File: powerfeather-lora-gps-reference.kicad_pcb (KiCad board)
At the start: 2 copper layers, 23.1 x 58.1 mm, 19 parts, among them J1 Conn_01x05, J10 Conn_01x01, J11 Conn_01x04, J2 Conn_01x02, J3 Conn_01x04, J4 Conn_01x02, J5 Conn_01x02, J6 Conn_01x04, J7 Conn_01x04, J8 Conn_01x03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

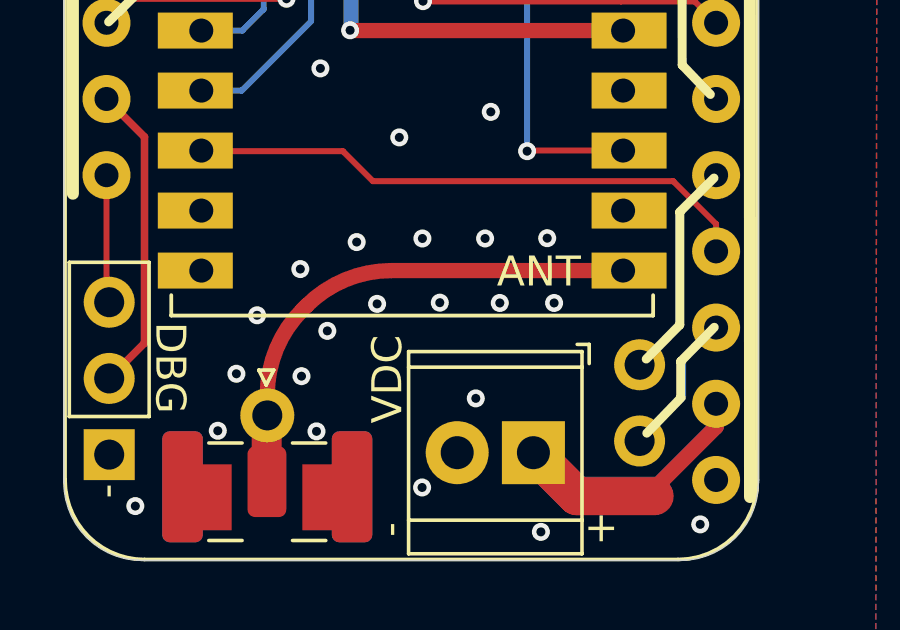
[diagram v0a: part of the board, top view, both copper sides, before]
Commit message: Change antenna trace width according to calc
- 4.5 dielectric constant
- H=1.6
- 865/920 Mhz
- S=0.5
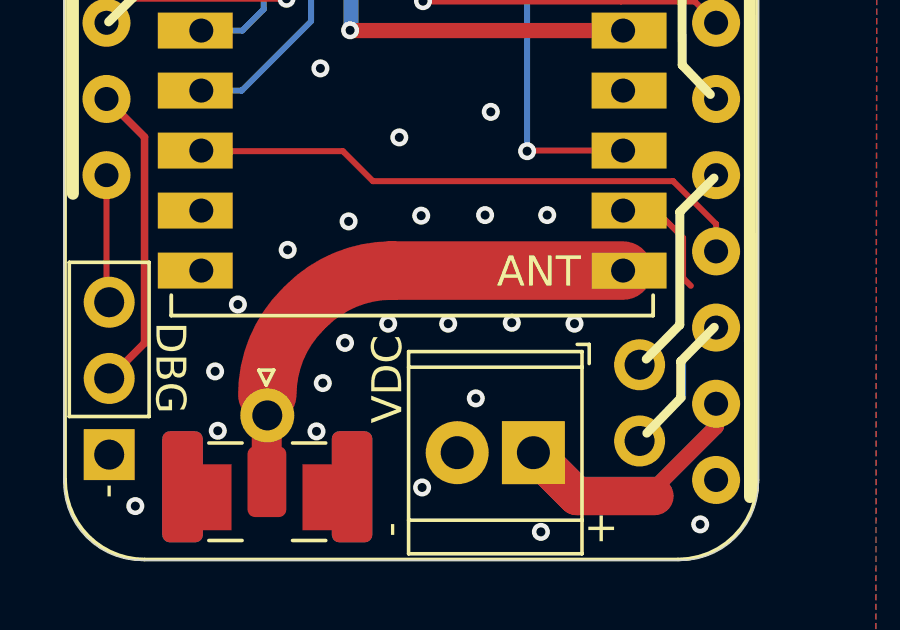
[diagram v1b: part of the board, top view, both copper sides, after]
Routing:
- net GND: track 2.11 -> 6.20 mm
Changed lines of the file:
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@@
+	)
+	(segment
+		(start 140.19 116.834365)
+		(end 140.19 118.18)
+		(width 0.2)
+		(layer "F.Cu")
+		(net 1)
+	)
+	(segment
+		(start 139.285635 115.93)
+		(end 140.19 116.834365)
+		(width 0.2)
+		(layer "F.Cu")
+		(net 1)
 	)
 	(segment
@@
 		(net 1)
 	)
-	(via
-		(at 129.99 119.04)
+	(segment
+		(start 138.19 115.93)
+		(end 139.285635 115.93)
+		(width 0.2)
+		(layer "F.Cu")
+		(net 1)
+	)
+	(segment
+		(start 140.19 118.18)
+		(end 140.45 118.44)
+		(width 0.2)
+		(layer "F.Cu")
+		(net 1)
+	)
+	(via
+		(at 130.36 119.7)
 		(size 0.6)
 		(drill 0.3)
@@
 	)
 	(via
-		(at 134.08 119.01)
+		(at 134.48 119.67)
 		(size 0.6)
 		(drill 0.3)
@@
 	)
 	(via
-		(at 129.31 116.98)
-		(size 0.6)
-		(drill 0.3)
-		(layers "F.Cu" "B.Cu")
-		(free yes)
-		(net 1)
-	)
-	(via
-		(at 128.33 119.94)
+		(at 129.04 116.29)
+		(size 0.6)
+		(drill 0.3)
+		(layers "F.Cu" "B.Cu")
+		(free yes)
+		(net 1)
+	)
+	(via
+		(at 128.92 120.34)
 		(size 0.6)
 		(drill 0.3)
@@
 	)
 	(via
-		(at 131.5 116.86)
+		(at 131.46 116.1)
 		(size 0.6)
 		(drill 0.3)
@@
 	)
 	(via
-		(at 135.89 119.01)
-		(size 0.6)
-		(drill 0.3)
-		(layers "F.Cu" "B.Cu")
-		(free yes)
-		(net 1)
-	)
-	(via
-		(at 133.59 116.86)
-		(size 0.6)
-		(drill 0.3)
-		(layers "F.Cu" "B.Cu")
-		(free yes)
-		(net 1)
-	)
-	(via
-		(at 127.43 117.88)
-		(size 0.6)
-		(drill 0.3)
-		(layers "F.Cu" "B.Cu")
-		(free yes)
-		(net 1)
-	)
-	(via
-		(at 135.66 116.85)
+		(at 136.57 119.7)
+		(size 0.6)
+		(drill 0.3)
+		(layers "F.Cu" "B.Cu")
+		(free yes)
+		(net 1)
+	)
+	(via
+		(at 133.59 116.08)
+		(size 0.6)
+		(drill 0.3)
+		(layers "F.Cu" "B.Cu")
+		(free yes)
+		(net 1)
+	)
+	(via
+		(at 127.01 117.24)
+		(size 0.6)
+		(drill 0.3)
+		(layers "F.Cu" "B.Cu")
+		(free yes)
+		(net 1)
+	)
+	(via
+		(at 135.66 116.08)
 		(size 0.6)
 		(drill 0.3)
@@
 	)
 	(via
-		(at 125.99 119.42)
+		(at 125.35 119.06)
 		(size 0.6)
 		(drill 0.3)
@@
 	)
 	(via
-		(at 132.08 119)
+		(at 132.36 119.7)
 		(size 0.6)
 		(drill 0.3)
@@
 	)
 	(via
-		(at 125.3 121.37)
-		(size 0.6)
-		(drill 0.3)
-		(layers "F.Cu" "B.Cu")
-		(free yes)
-		(net 1)
-	)
-	(via
-		(at 127.47 121.45)
+		(at 124.59 121.29)
+		(size 0.6)
+		(drill 0.3)
+		(layers "F.Cu" "B.Cu")
+		(free yes)
+		(net 1)
+	)
+	(via
+		(at 128.18 121.68)
 		(size 0.6)
 		(drill 0.3)
@@
 		(start 138.19 117.93)
 		(end 130.466854 117.93)
-		(width 0.508)
+		(width 1.95)
 		(layer "F.Cu")
 		(net 25)
@@
 		(mid 126.634482 120.53612)
 		(end 126.33 122.066854)
-		(width 0.508)
+		(width 1.95)
 		(layer "F.Cu")
 		(net 25)
@@
 		(mid 128.93612 118.234482)
 		(end 130.466854 117.93)
-		(width 0.508)
+		(width 1.95)
 		(layer "F.Cu")
 		(net 25)
